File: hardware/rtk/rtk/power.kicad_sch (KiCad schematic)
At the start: 23 parts, among them J1 USB4105-GF-A, J2 USB4105-GF-A, J3 B2B-PH-SM4-TBLFSN, J4 Conn_01x02_Pin, U1 BQ24075RGT, U2 TPS63020DSJR

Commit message: Schematic progress: all sheets ~90% complete (#182)
- power.kicad_sch: PSU, BQ24075, LiPo connector, USB-C power path
- stm32f765vit.kicad_sch: F765VIT pin assignments, SPI2/I2C4/SDMMC1/UART7/8/USART3
- usb2hs.kicad_sch: USB3300 ULPI, 24MHz TCXO (ASTX-H11-24MHz), USB-C connector, diff pair nets USB_D+/USB_D-
- zed-f9p-05b.kicad_sch: ZED-F9P-05B connections
- rtk-base.ioc: DIO1 corrected to GPIO_Input, LSM6DSOX CS removed (I2C mode, CS tied high in schematic), DIO2 label typo fixed
- rtk.kicad_pcb/pro: project settings updated

Co-Authored-By: Claude Sonnet 4.6 <noreply@anthropic.com>
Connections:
- net USB_D_P: now reaches J1.A6 (DP1)
- net USB_D_P: now also J1.B6 (DP2)
- net USB_D_N: now reaches J1.A7 (DN1)
- net USB_D_N: now also J1.B7 (DN2)
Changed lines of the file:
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@@
+	)
+	(junction
+		(at 31.75 39.37)
+		(diameter 0)
+		(color 0 0 0 0)
 	)
 	(junction
@@
 	(junction
 		(at 29.21 74.93)
+		(diameter 0)
+		(color 0 0 0 0)
+	)
+	(junction
+		(at 81.28 46.99)
 		(diameter 0)
 		(color 0 0 0 0)
@@
 	(wire
 		(pts
+			(xy 36.83 41.91) (xy 31.75 41.91)
+		)
+		(stroke
+			(width 0)
+			(type default)
+		)
+	)
+	(wire
+		(pts
 			(xy 152.4 66.04) (xy 152.4 68.58)
 		)
@@
 	(wire
 		(pts
+			(xy 31.75 39.37) (xy 31.75 41.91)
+		)
+		(stroke
+			(width 0)
+			(type default)
+		)
+	)
+	(wire
+		(pts
 			(xy 229.87 72.39) (xy 237.49 72.39)
 		)
@@
 	(wire
 		(pts
+			(xy 31.75 39.37) (xy 36.83 39.37)
+		)
+		(stroke
+			(width 0)
+			(type default)
+		)
+	)
+	(wire
+		(pts
 			(xy 245.11 142.24) (xy 252.73 142.24)
 		)
@@
 	(wire
 		(pts
+			(xy 26.67 39.37) (xy 31.75 39.37)
+		)
+		(stroke
+			(width 0)
+			(type default)
+		)
+	)
+	(wire
+		(pts
 			(xy 157.48 55.88) (xy 162.56 55.88)
 		)
@@
 	(wire
 		(pts
+			(xy 77.47 46.99) (xy 81.28 46.99)
+		)
+		(stroke
+			(width 0)
+			(type default)
+		)
+	)
+	(wire
+		(pts
 			(xy 30.48 132.08) (xy 30.48 134.62)
 		)
@@
 	(wire
 		(pts
+			(xy 81.28 46.99) (xy 86.36 46.99)
+		)
+		(stroke
+			(width 0)
+			(type default)
+		)
+	)
+	(wire
+		(pts
 			(xy 138.43 45.72) (xy 125.73 45.72)
 		)
@@
 	(wire
 		(pts
+			(xy 77.47 49.53) (xy 81.28 49.53)
+		)
+		(stroke
+			(width 0)
+			(type default)
+		)
+	)
+	(wire
+		(pts
 			(xy 175.26 71.12) (xy 175.26 78.74)
 		)
@@
 		(pts
 			(xy 262.89 138.43) (xy 262.89 142.24)
+		)
+		(stroke
+			(width 0)
+			(type default)
+		)
+	)
+	(wire
+		(pts
+			(xy 81.28 49.53) (xy 81.28 46.99)
 		)
 		(stroke
@@
 		)
 	)
+	(global_label "USB_D_N"
+		(shape input)
+		(at 26.67 39.37 180)
+		(fields_autoplaced yes)
+		(effects
+			(font
+				(size 1.27 1.27)
+			)
+			(justify right)
+		)
+		(property "Intersheetrefs" "${INTERSHEET_REFS}"
+			(at 15.3391 39.37 0)
+			(hide yes)
+			(show_name no)
+			(do_not_autoplace no)
+			(effects
+				(font
+					(size 1.27 1.27)
+				)
+				(justify right)
+			)
+		)
+	)
 	(global_label "BQ24975_EN2"
 		(shape input)
@@
 			)
 		)
+	)
+	(global_label "USB_D_P"
+		(shape input)
+		(at 86.36 46.99 0)
+		(fields_autoplaced yes)
+		(effects
+			(font
+				(size 1.27 1.27)
+			)
+			(justify left)
+		)
+		(property "Intersheetrefs" "${INTERSHEET_REFS}"
+			(at 97.6304 46.99 0)
+			(hide yes)
+			(show_name no)
+			(do_not_autoplace no)
+			(effects
+				(font
+					(size 1.27 1.27)
+				)
+				(justify left)
+			)
+		)

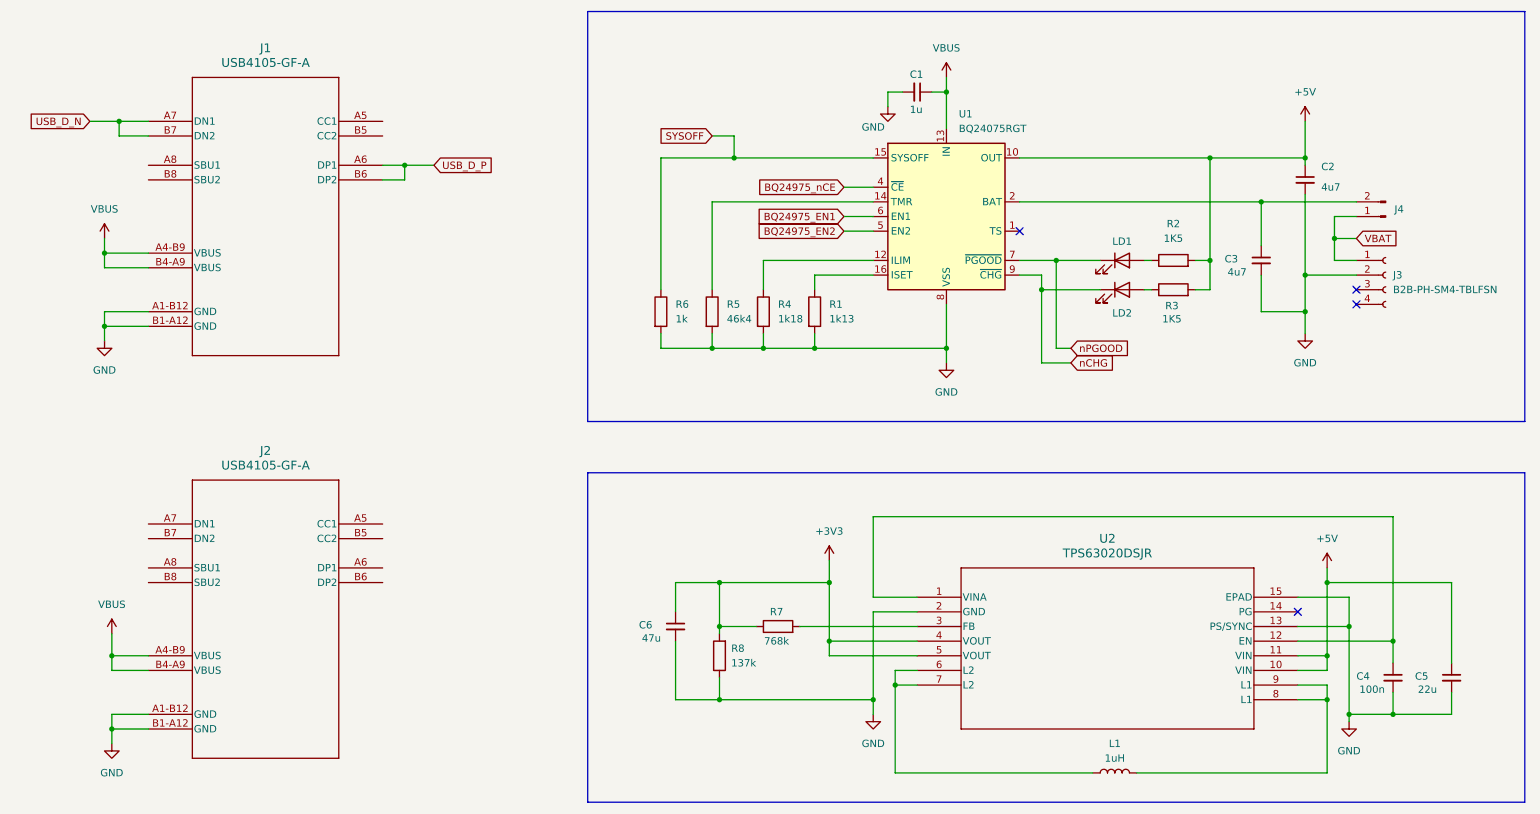
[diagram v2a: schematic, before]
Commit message: Power sheet review fixes; SLVA553 inrush mitigation added (#182)
- power.kicad_sch: CC1/CC2 5.1k pull-downs on J1+J2, FB divider wiring
  fixed, TPS63020 inrush D1+C_SS per SLVA553, 1M NF bleed resistor
  across C_SS, TS NF 82k5 resistor added, nPGOOD/nCHG net labels added
- stm32f765vit.kicad_sch: nPGOOD→PD10, nCHG→PD11, SYSOFF→PD7 inputs added
- firmware/rtk-base/rtk-base.ioc: PD7/PD10/PD11 assigned
- docs/datasheets/slva553.pdf: TI SLVA553 app note (TPS6302x inrush)

Co-Authored-By: Claude Sonnet 4.6 <noreply@anthropic.com>
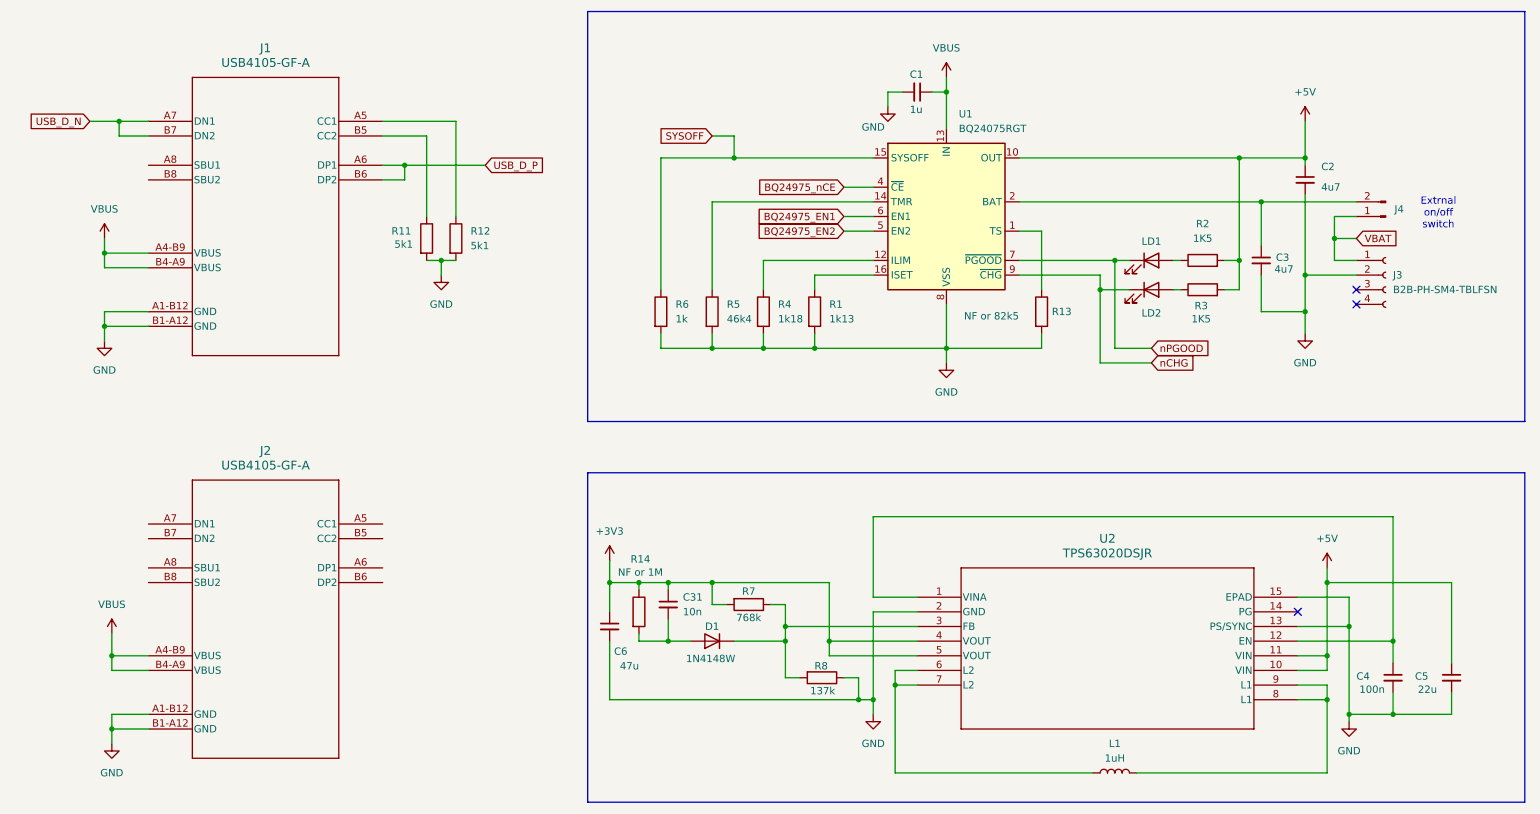
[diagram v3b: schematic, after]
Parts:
- added C31: 10n, Capacitor_SMD:C_0805_2012Metric_Pad1.18x1.45mm_HandSolder, symbol Device:C_Small
- added D1: 1N4148W, Diode_SMD:D_SOD-123, symbol Diode:1N4148W
- added R11, R12: 5k1, Resistor_SMD:R_0805_2012Metric_Pad1.20x1.40mm_HandSolder, symbol Device:R
- added R13: NF or 82k5, Resistor_SMD:R_0805_2012Metric_Pad1.20x1.40mm_HandSolder, symbol Device:R
- added R14: NF or 1M, Resistor_SMD:R_0805_2012Metric_Pad1.20x1.40mm_HandSolder, symbol Device:R
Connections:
- net +3V3: now also R7.2, C31.1, R14.1; no longer R7.1, R8.2
- net GND: now also R11.2, R12.2, R13.2
- net at U2.3 (FB): now also R7.1, R8.2, D1.1 (K); no longer R7.2
- net at J1.A5 (CC1): now also R12.1
- net at J1.B5 (CC2): now also R11.1
- net at U1.1 (TS): now also R13.1
- new net: C31.2, D1.2 (A), R14.2
- no-connect marks 4 -> 3
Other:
- note added: "Extrnal on/off switch"
- moved on the sheet: C6, LD1, LD2, R2, R3, R7, R8

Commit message: STM32F765VIT sheet review fixes (#182)
- VBAT tied to +3V3 (not raw LiPo)
- CORE1262 RXEN/TXEN reassigned to PC6/PC7 GPIO outputs (init low)
- I2C4 external 4k7 pull-ups added on SCL/SDA
- BOOT0 pull-down + test point added
- LSM6DSOX CS tied to +3V3, SDO/SA0 tied to GND (addr 0x6A)
- ESP32-S3-ZERO: 5V NC, powered via 3V3 rail; GP1-GP5 wired to PE2-PE6
- nPGOOD/nCHG/SYSOFF added to STM32 sheet
- MMC5603NJ sub-board connector added (I2C4, 2x GPIO, 3V3, GND)
- rtk-base.ioc: PC6/PC7 RXEN/TXEN, PE2-PE6 spare, PD7/PD10/PD11

Co-Authored-By: Claude Sonnet 4.6 <noreply@anthropic.com>
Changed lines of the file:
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@@
-	)
-	(junction
-		(at 242.57 59.69)
-		(diameter 0)
-		(color 0 0 0 0)
 	)
 	(junction
@@
 	(wire
 		(pts
-			(xy 242.57 59.69) (xy 242.57 63.5)
+			(xy 242.57 55.88) (xy 242.57 63.5)
 		)
 		(stroke
@@
 	(wire
 		(pts
-			(xy 242.57 55.88) (xy 242.57 59.69)
-		)
-		(stroke
-			(width 0)
-			(type default)
-		)
-	)
-	(wire
-		(pts
 			(xy 85.09 63.5) (xy 87.63 63.5)
 		)
@@
 	(wire
 		(pts
-			(xy 242.57 59.69) (xy 246.38 59.69)
-		)
-		(stroke
-			(width 0)
-			(type default)
-		)
-	)
-	(wire
-		(pts
 			(xy 191.77 58.42) (xy 187.96 58.42)
 		)
@@
 			(width 0)
 			(type default)
+		)
+	)
+	(label "VBAT"
+		(at 242.57 60.96 0)
+		(effects
+			(font
+				(size 1.27 1.27)
+			)
+			(justify left bottom)
 		)
 	)
@@
 			(hide yes)
 			(show_name no)
-			(do_not_autoplace no)
-			(effects
-				(font
-					(size 1.27 1.27)
-				)
-				(justify left)
-			)
-		)
-	)
-	(global_label "VBAT"
-		(shape input)
-		(at 246.38 59.69 0)
-		(fields_autoplaced yes)
-		(effects
-			(font
-				(size 1.27 1.27)
-			)
-			(justify left)
-		)
-		(property "Intersheetrefs" "${INTERSHEET_REFS}"
-			(at 253.78 59.69 0)
-			(hide yes)
-			(show_name no)

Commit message: ZED-F9P sheet review fixes (#182)
- V_BCKP tied to +3V3 with 100nF decoupling
- VCC decoupling caps added on module side of L2/L3
- SAFEBOOT_N and RESET_N 10k pull-ups to +3V3 added
- L3 on VCC_RF replaced with ferrite bead (600R at 100MHz)

Co-Authored-By: Claude Sonnet 4.6 <noreply@anthropic.com>
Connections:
- net USB_D_N renamed USB_D2_N
- net USB_D_P renamed USB_D2_P
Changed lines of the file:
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@@
 		)
 	)
-	(global_label "USB_D_N"
+	(global_label "USB_D2_N"
 		(shape input)
 		(at 26.67 39.37 180)
@@
 		)
 		(property "Intersheetrefs" "${INTERSHEET_REFS}"
-			(at 15.3391 39.37 0)
+			(at 14.1296 39.37 0)
 			(hide yes)
 			(show_name no)
@@
 		)
 	)
-	(global_label "USB_D_P"
+	(global_label "USB_D2_P"
 		(shape input)
 		(at 95.25 46.99 0)
@@
 		)
 		(property "Intersheetrefs" "${INTERSHEET_REFS}"
-			(at 106.5204 46.99 0)
+			(at 107.7299 46.99 0)
 			(hide yes)
 			(show_name no)

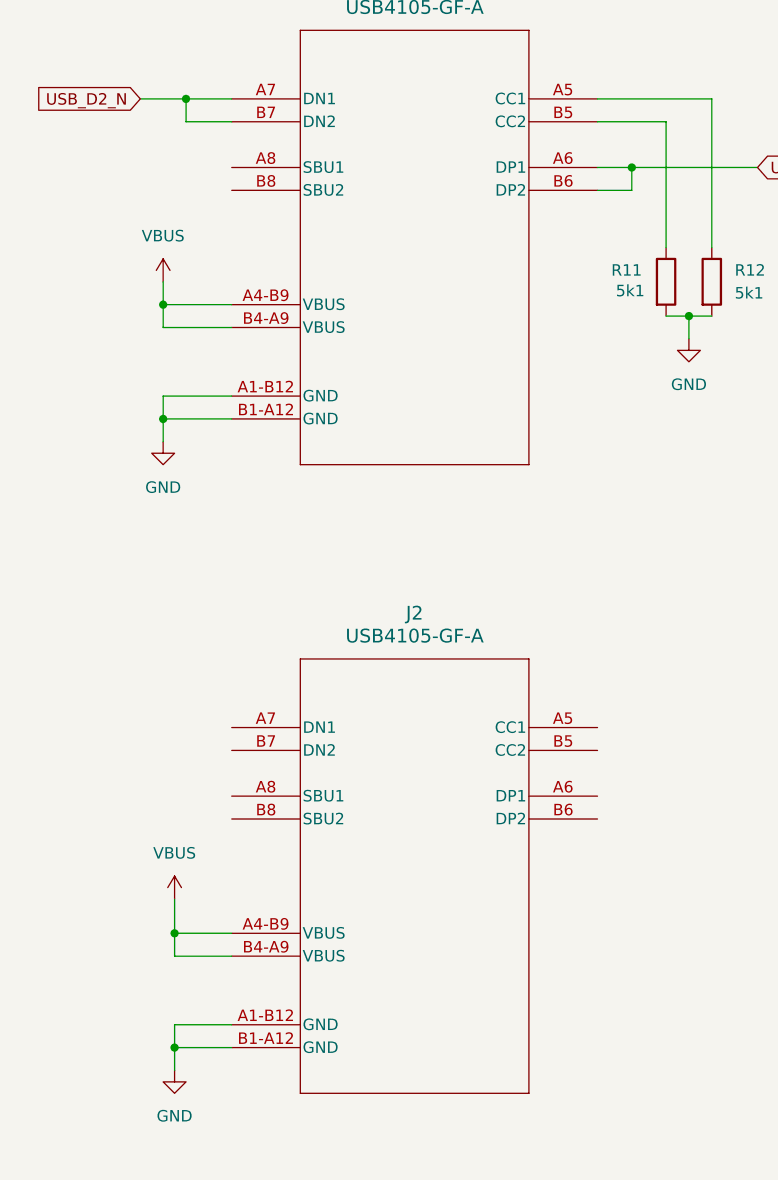
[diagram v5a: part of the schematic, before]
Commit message: Full schematic review complete — final fixes (#182)
- power.kicad_sch: J2 USB-C removed (J1 covers both power and data),
  CC1/CC2 5k1 pull-downs on J1 confirmed
- usb2hs.kicad_sch: VDD1.8 decoupling updated to 470nF, ESD TVS added
- stm32f765vit.kicad_sch: misc cleanup from review
- zed-f9p-05b.kicad_sch: V_BCKP, decoupling, pull-ups, ferrite bead fixes

Co-Authored-By: Claude Sonnet 4.6 <noreply@anthropic.com>
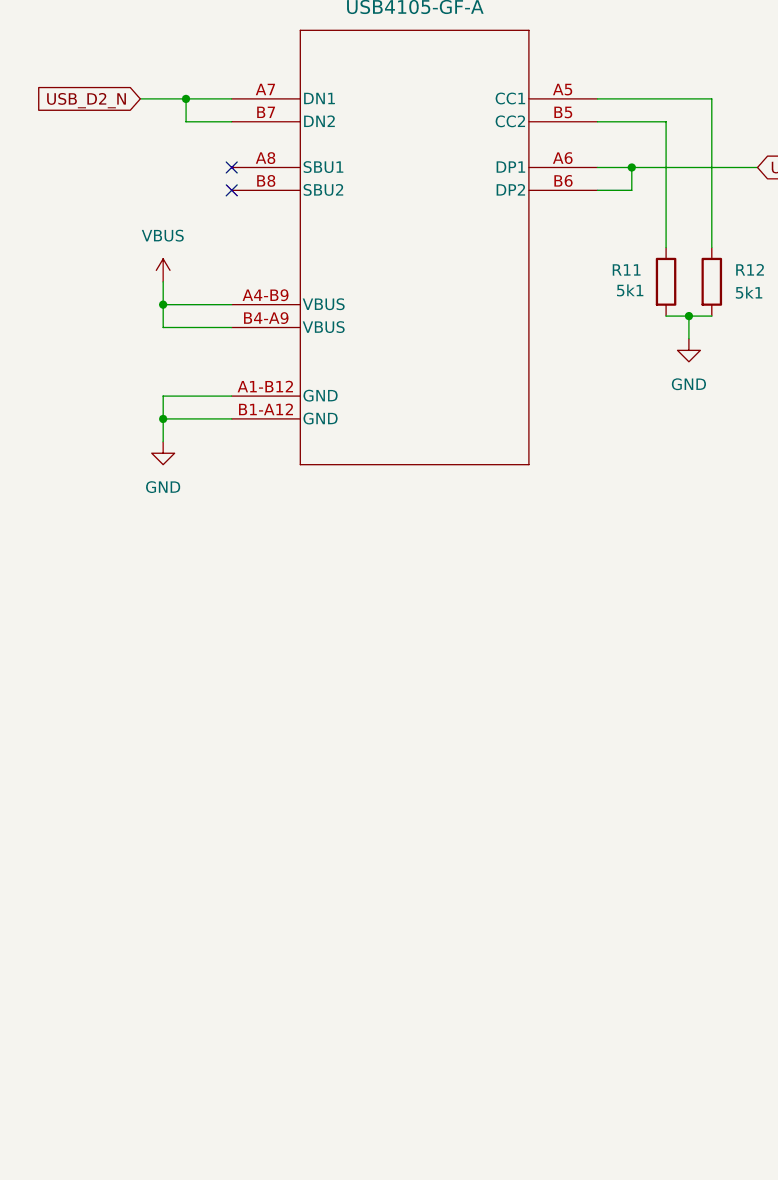
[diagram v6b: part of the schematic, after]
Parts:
- removed J2: USB4105-GF-A, USB4105_GCT, symbol USB4105-GF-A-060:USB4105-GF-A
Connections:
- no-connect marks 3 -> 5
